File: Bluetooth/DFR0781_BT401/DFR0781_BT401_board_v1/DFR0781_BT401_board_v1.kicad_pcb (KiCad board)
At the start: 2 copper layers, 40.5 x 23.5 mm, 8 parts, among them J1 PINHD_1x8_Female

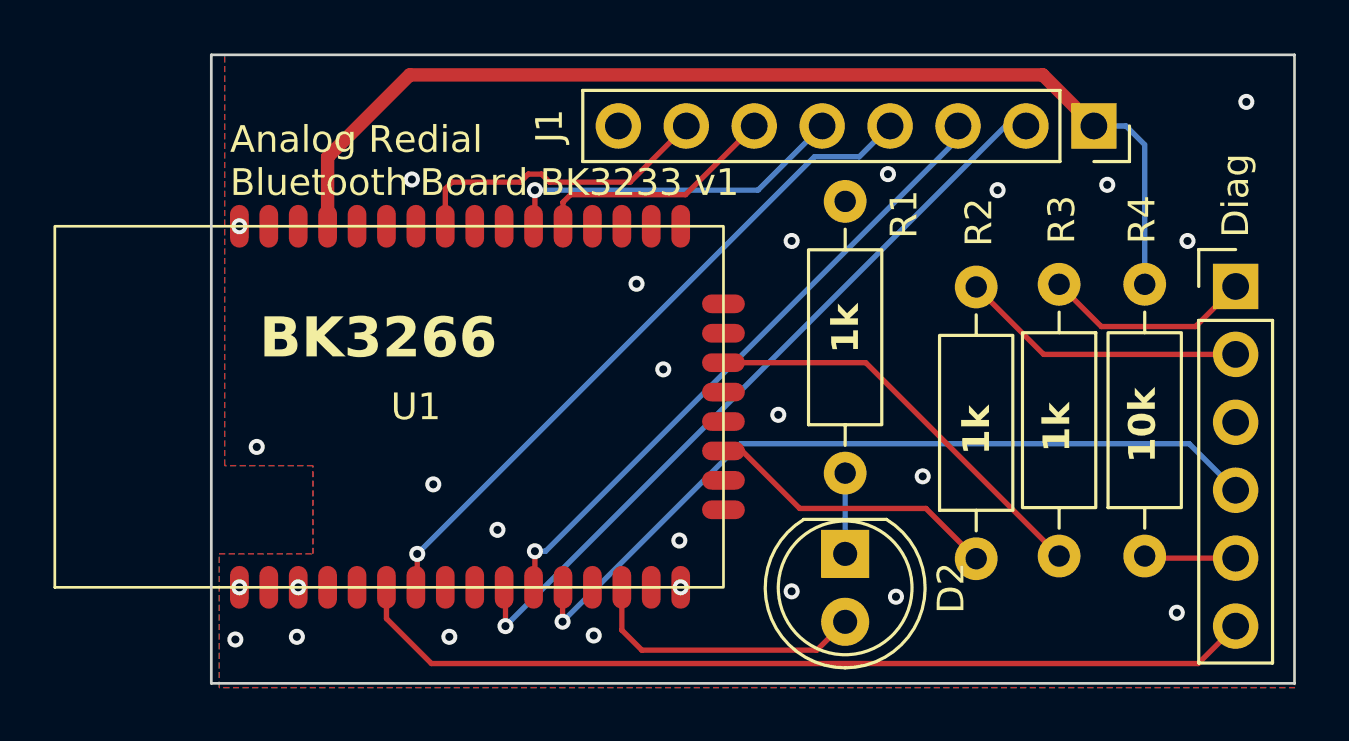
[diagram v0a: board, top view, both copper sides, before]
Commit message: BT401 adapter board v1 released for fab (C1 to GND, reset and DACR on J2); docs: designed, not yet built or tested
Co-Authored-By: Claude Opus 5.5 <noreply@anthropic.com>
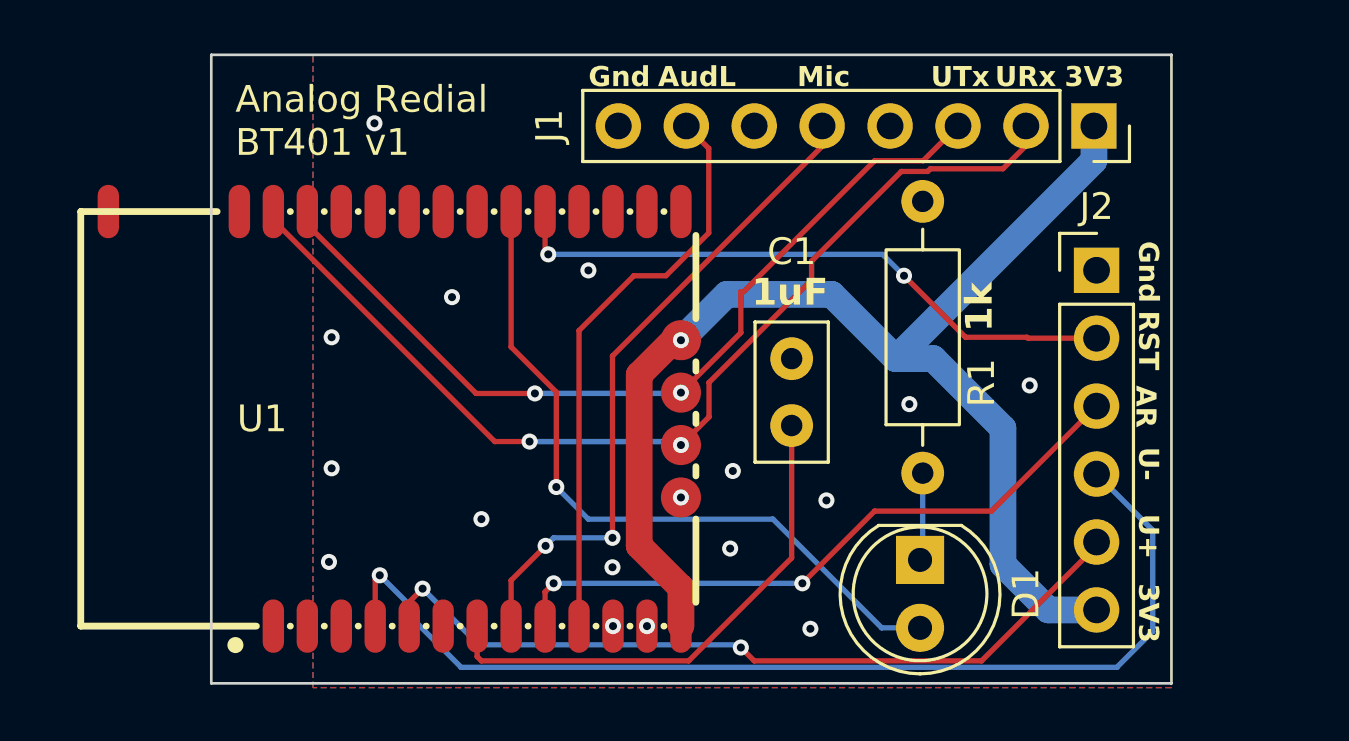
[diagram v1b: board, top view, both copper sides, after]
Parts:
- removed D2: LED_5mm, LED_THT:LED_D5.0mm
- removed Diag: PINHD_1x6_Male, Connector_PinHeader_2.54mm:PinHeader_1x06_P2.54mm_Vertical
- removed R2, R3: 1k, Resistor_THT:R_Axial_DIN0207_L6.3mm_D2.5mm_P10.16mm_Horizontal
- removed R4: 10k, Resistor_THT:R_Axial_DIN0207_L6.3mm_D2.5mm_P10.16mm_Horizontal
- added C1: 1uF 105_Ceramic, Capacitor_THT:C_Disc_D5.0mm_W2.5mm_P2.50mm, F.Cu at (138.9, 87.9)
- added D1: LED_5mm, LED_THT:LED_D5.0mm, F.Cu at (143.7, 92.9)
- added J2: PINHD_1x6_Male, Connector_PinHeader_2.54mm:PinHeader_1x06_P2.54mm_Vertical, F.Cu at (150.3, 82.1)
- U1: footprint Custom:BK3266SR -> Custom:DFR0781_BT401_new
- moved R1 2.90 mm to (143.8, 89.7)
- moved U1 1.93 mm to (119.5, 95.4)
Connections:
- J1 pad 4: /Wake -> unconnected-(J1-Pad4)
- J1 pad 6: /Mic_N1 -> unconnected-(J1-Pad6)
- U1 pad 1: GND -> unconnected-(U1-PA3/AUX1L/PWM0/Uart-Tx-Pad1)
- U1 pad 10: /espUartRx -> /AudioLP
- U1 pad 11: /espUartTx -> GND
- U1 pad 12: Net-(U1-Mode_(GPIO7)#1) -> GND
- U1 pad 13: unconnected-(U1-S/R_(GPIO6)#1-Pad13) -> +3.3V
- U1 pad 14: Net-(U1-LED_(GPIO8)) -> unconnected-(U1-GPIO/PWM1/PC1-Pad14)
- U1 pad 16: GND -> unconnected-(U1-SDCMD/PC4-Pad16)
- U1 pad 18: unconnected-(U1-SD_CMD_(GPIO12)-Pad18) -> /Reset
- U1 pad 22: Net-(U1-S/R_(GPIO6)#2) -> unconnected-(U1-GPIO/PB4-Pad22)
- U1 pad 25: unconnected-(U1-GND-Pad25) -> /espUartTx
- U1 pad 26: unconnected-(U1-GPIO3-Pad26) -> /espUartRx
- U1 pad 3: GND -> unconnected-(U1-PA5/ADKEY-Pad3)
- U1 pad 4: unconnected-(U1-Prev/Vol-_(GPIO14)-Pad4) -> /USBDM
- U1 pad 5: unconnected-(U1-Next/Vol+_(GPIO5)-Pad5) -> /USBDP
- U1 pad 6: /PP_Call -> unconnected-(U1-3V3-Pad6)
- U1 pad 7: /Wake -> Net-(U1-DVDD)
- U1 pad 8: unconnected-(U1-NC-Pad8) -> /Mic_P1
- U1 pad 9: unconnected-(U1-NC-Pad9) -> /AudioRP
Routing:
- net /USBDM: track 0.00 -> 39.8 mm, vias 0 -> 1
- net /PP_Call: track 34.2 -> 0.00 mm
- net Net-(U1-Mode_(GPIO7)#1): track 29.9 -> 0.00 mm, vias 1 -> 0
- net /USBDP: track 0.00 -> 29.9 mm, vias 0 -> 2
- net /Wake: track 25.6 -> 0.00 mm, vias 1 -> 0
- net /AudioRP: track 0.00 -> 24.8 mm, vias 0 -> 2
- net /Reset: track 0.00 -> 23.4 mm, vias 0 -> 2
- net Net-(U1-DVDD): track 0.00 -> 19.5 mm
- net Net-(U1-LED/PR1): track 11.1 -> 26.8 mm, vias 0 -> 1
- net Net-(U1-S/R_(GPIO6)#2): track 15.5 -> 0.00 mm
- net /Mic_P1: track 13.1 -> 24.8 mm, vias 1 -> 2
- net Net-(J2-Pad2): track 10.7 -> 0.00 mm
- net Net-(U1-LED_(GPIO8)): track 10.7 -> 0.00 mm
- net /AudioLP: track 11.6 -> 21.8 mm
- net /espUartRx: track 28.7 -> 38.5 mm, vias 1 -> 2
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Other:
- board size 40.5 x 23.5 mm -> 35.9 x 23.5 mm
- board text added: "1uF"
- board text added: "3V3"
- board text added: "AR"
- board text added: "Analog Redial BT401 v1"
- board text added: "AudL"
- board text added: "DFR0781 BT401 Bluetooth Board V1"
- board text added: "Gnd"
- board text added: "Mic"
- board text added: "RST"
- board text added: "U+"
- board text added: "U-"
- board text added: "URx"
- board text added: "UTx"
- board text removed: "10k"
- board text removed: "Analog Redial Bluetooth Board 1"
- board text removed: "Analog Redial Bluetooth Board BK3233 v1"
- board text removed: "BK3266"
